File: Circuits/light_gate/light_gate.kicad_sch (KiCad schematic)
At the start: 11 parts, among them Q1 BC547

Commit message: udated footprints npn
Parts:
- H1: value (none) -> MountingHole; footprint (none) -> MountingHole:MountingHole_2.2mm_M2_DIN965
- H2: footprint (none) -> MountingHole:MountingHole_2.2mm_M2_DIN965
- J1: value (none) -> Conn_01x03; footprint (none) -> Connector_PinHeader_2.54mm:PinHeader_1x03_P2.54mm_Vertical
- J2: value (none) -> Conn_01x02; footprint (none) -> Connector_PinHeader_2.54mm:PinHeader_1x02_P2.54mm_Vertical
- Q1: footprint Package_TO_SOT_THT:TO-92_Inline -> (none)
- R1: value (none) -> 220; footprint (none) -> Resistor_THT:R_Axial_DIN0207_L6.3mm_D2.5mm_P7.62mm_Horizontal
- R2: value (none) -> 470k; footprint (none) -> Resistor_THT:R_Axial_DIN0207_L6.3mm_D2.5mm_P7.62mm_Horizontal
- R3: value (none) -> 10; footprint (none) -> Resistor_THT:R_Axial_DIN0207_L6.3mm_D2.5mm_P7.62mm_Horizontal
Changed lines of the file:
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@@
     (in_bom yes) (on_board yes) (fields_autoplaced)
     (property "Reference" "J2" (id 0) (at 120.65 49.53 0))
-    (property "Value" "" (id 1) (at 120.65 52.07 0))
-    (property "Footprint" "" (id 2) (at 120.65 58.42 0)
+    (property "Value" "Conn_01x02" (id 1) (at 120.65 52.07 0))
+    (property "Footprint" "Connector_PinHeader_2.54mm:PinHeader_1x02_P2.54mm_Vertical" (id 2) (at 120.65 58.42 0)
       (effects (font (size 1.27 1.27)) hide)
     )
@@
       (effects (font (size 1.27 1.27)) (justify left))
     )
-    (property "Footprint" "Package_TO_SOT_THT:TO-92_Inline" (id 2) (at 110.49 60.325 0)
+    (property "Footprint" "" (id 2) (at 110.49 60.325 0)
       (effects (font (size 1.27 1.27) italic) (justify left) hide)
     )
@@
       (effects (font (size 1.27 1.27)) (justify left))
     )
-    (property "Value" "" (id 1) (at 102.87 53.3399 0)
-      (effects (font (size 1.27 1.27)) (justify left))
-    )
-    (property "Footprint" "" (id 2) (at 98.552 52.07 90)
+    (property "Value" "10" (id 1) (at 102.87 53.3399 0)
+      (effects (font (size 1.27 1.27)) (justify left))
+    )
+    (property "Footprint" "Resistor_THT:R_Axial_DIN0207_L6.3mm_D2.5mm_P7.62mm_Horizontal" (id 2) (at 98.552 52.07 90)
       (effects (font (size 1.27 1.27)) hide)
     )
@@
       (effects (font (size 1.27 1.27)) (justify left))
     )
-    (property "Footprint" "" (id 2) (at 74.93 43.18 0)
+    (property "Footprint" "MountingHole:MountingHole_2.2mm_M2_DIN965" (id 2) (at 74.93 43.18 0)
       (effects (font (size 1.27 1.27)) hide)
     )
@@
       (effects (font (size 1.27 1.27)) (justify left))
     )
-    (property "Value" "" (id 1) (at 95.25 53.3399 0)
-      (effects (font (size 1.27 1.27)) (justify left))
-    )
-    (property "Footprint" "" (id 2) (at 90.932 52.07 90)
+    (property "Value" "470k" (id 1) (at 95.25 53.3399 0)
+      (effects (font (size 1.27 1.27)) (justify left))
+    )
+    (property "Footprint" "Resistor_THT:R_Axial_DIN0207_L6.3mm_D2.5mm_P7.62mm_Horizontal" (id 2) (at 90.932 52.07 90)
       (effects (font (size 1.27 1.27)) hide)
     )
@@
     (in_bom yes) (on_board yes) (fields_autoplaced)
     (property "Reference" "J1" (id 0) (at 68.58 49.53 0))
-    (property "Value" "" (id 1) (at 68.58 52.07 0))
-    (property "Footprint" "" (id 2) (at 68.58 58.42 0)
+    (property "Value" "Conn_01x03" (id 1) (at 68.58 52.07 0))
+    (property "Footprint" "Connector_PinHeader_2.54mm:PinHeader_1x03_P2.54mm_Vertical" (id 2) (at 68.58 58.42 0)
       (effects (font (size 1.27 1.27)) hide)
     )
@@
       (effects (font (size 1.27 1.27)) (justify left))
     )
-    (property "Value" "" (id 1) (at 115.57 43.18 0)
-      (effects (font (size 1.27 1.27)) (justify left))
-    )
-    (property "Footprint" "" (id 2) (at 115.57 43.18 0)
+    (property "Value" "MountingHole" (id 1) (at 115.57 43.18 0)
+      (effects (font (size 1.27 1.27)) (justify left))
+    )
+    (property "Footprint" "MountingHole:MountingHole_2.2mm_M2_DIN965" (id 2) (at 115.57 43.18 0)
       (effects (font (size 1.27 1.27)) hide)
     )
@@
       (effects (font (size 1.27 1.27)) (justify left))
     )
-    (property "Value" "" (id 1) (at 86.36 53.3399 0)
-      (effects (font (size 1.27 1.27)) (justify left))
-    )
-    (property "Footprint" "" (id 2) (at 82.042 52.07 90)
+    (property "Value" "220" (id 1) (at 86.36 53.3399 0)
+      (effects (font (size 1.27 1.27)) (justify left))
+    )
+    (property "Footprint" "Resistor_THT:R_Axial_DIN0207_L6.3mm_D2.5mm_P7.62mm_Horizontal" (id 2) (at 82.042 52.07 90)
       (effects (font (size 1.27 1.27)) hide)
     )
@@
     )
     (path "/10e50957-8ccb-462c-a1ab-2c68753f4dff"
-      (reference "Q1") (unit 1) (value "BC547") (footprint "Package_TO_SOT_THT:TO-92_Inline")
+      (reference "Q1") (unit 1) (value "BC547") (footprint "Package_TO_SOT_THT:TO-92L_Inline_Wide")
     )
     (path "/e8d8bbd4-2e6c-40b0-92e3-9d9c5a98e195"

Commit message: changed circuit
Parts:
- R3: value 10 -> 10k
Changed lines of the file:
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@@
       (effects (font (size 1.27 1.27)) (justify left))
     )
-    (property "Value" "10" (id 1) (at 102.87 53.3399 0)
+    (property "Value" "10k" (id 1) (at 102.87 53.3399 0)
       (effects (font (size 1.27 1.27)) (justify left))
     )
@@
     )
     (path "/10e50957-8ccb-462c-a1ab-2c68753f4dff"
-      (reference "Q1") (unit 1) (value "BC547") (footprint "Package_TO_SOT_THT:TO-92L_Inline_Wide")
+      (reference "Q1") (unit 1) (value "BC547") (footprint "Package_TO_SOT_THT:TO-92L_HandSolder")
     )
     (path "/e8d8bbd4-2e6c-40b0-92e3-9d9c5a98e195"
@@
     )
     (path "/1f796a2c-0195-444a-b957-72363cb03819"
-      (reference "R3") (unit 1) (value "10") (footprint "Resistor_THT:R_Axial_DIN0207_L6.3mm_D2.5mm_P7.62mm_Horizontal")
+      (reference "R3") (unit 1) (value "10k") (footprint "Resistor_THT:R_Axial_DIN0207_L6.3mm_D2.5mm_P7.62mm_Horizontal")
     )
   )

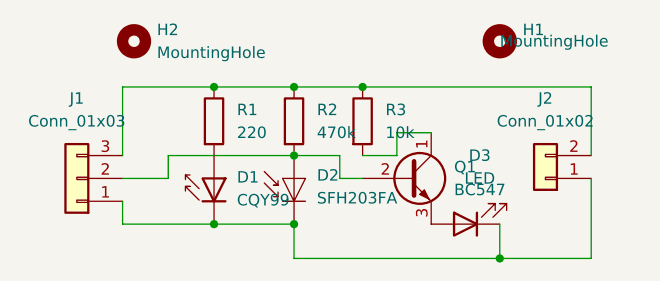
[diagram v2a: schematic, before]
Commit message: added lm393 to lightgate
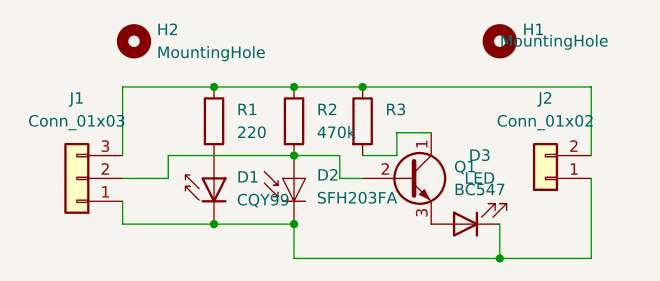
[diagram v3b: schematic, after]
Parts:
- Q1: footprint (none) -> Package_TO_SOT_THT:TO-92L_HandSolder
- R3: value 10k -> (none)
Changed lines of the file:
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@@
       (effects (font (size 1.27 1.27)) (justify left))
     )
-    (property "Footprint" "" (id 2) (at 110.49 60.325 0)
+    (property "Footprint" "Package_TO_SOT_THT:TO-92L_HandSolder" (id 2) (at 110.49 60.325 0)
       (effects (font (size 1.27 1.27) italic) (justify left) hide)
     )
@@
       (effects (font (size 1.27 1.27)) (justify left))
     )
-    (property "Value" "10k" (id 1) (at 102.87 53.3399 0)
+    (property "Value" "" (id 1) (at 102.87 53.3399 0)
       (effects (font (size 1.27 1.27)) (justify left))
     )
@@
     )
     (path "/1f796a2c-0195-444a-b957-72363cb03819"
-      (reference "R3") (unit 1) (value "10k") (footprint "Resistor_THT:R_Axial_DIN0207_L6.3mm_D2.5mm_P7.62mm_Horizontal")
+      (reference "R3") (unit 1) (value "100") (footprint "Resistor_THT:R_Axial_DIN0207_L6.3mm_D2.5mm_P7.62mm_Horizontal")
     )
   )
